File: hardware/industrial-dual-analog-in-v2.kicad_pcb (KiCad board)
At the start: 2 copper layers, 40 x 40 mm, 81 parts, among them P1 CON-SENSOR2, P2 CONN_1, P3 CONN_8, P4 DEBUG, P5 DEBUG, U1 LMV342IDRG4, U2 LM2664, U3 XMC1XXX24, U4 MCP3911, U5 DRILL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

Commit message: fix origin, fix logos
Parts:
- moved G*** 16.2 mm to (145.6, 100.0), turned to 90 degrees
- moved VAL 16.2 mm to (125.6, 100.0), turned to 90 degrees
- moved VAL 16.2 mm to (135.6, 100.0), turned to 90 degrees
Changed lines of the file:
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@@
-(kicad_pcb (version 4) (host pcbnew 4.0.7-e2-6376~58~ubuntu17.04.1)
+(kicad_pcb (version 4) (host pcbnew 4.0.7-e2-6376~61~ubuntu18.04.1)
   (general
     (links 158)
@@
     (pad_drill 0)
     (pad_to_mask_clearance 0.2)
-    (aux_axis_origin 0 0)
+    (aux_axis_origin 115.6 80)
+    (grid_origin 115.6 80)
     (visible_elements FFFFEF3F)
     (pcbplotparams
@@
     (descr "module 1 pin (ou trou mecanique de percage)")
     (tags DEV)
-    (fp_text reference P2 (at 0 -1.26746) (layer F.SilkS)
+    (fp_text reference P2 (at 0.8 -0.95) (layer F.SilkS) hide
       (effects (font (size 0.508 0.508) (thickness 0.127)))
     )
@@
   )
   (module kicad-libraries:CE_5mm (layer B.Cu)
-    (at 125.1 116.2 270)
-    (fp_text reference VAL (at 0 0 270) (layer B.SilkS) hide
+    (at 125.6 100 90)
+    (fp_text reference VAL (at 0 0 90) (layer B.SilkS) hide
       (effects (font (size 0.2 0.2) (thickness 0.05)) (justify mirror))
     )
-    (fp_text value CE_5mm (at 0 0 270) (layer B.SilkS) hide
+    (fp_text value CE_5mm (at 0 0 90) (layer B.SilkS) hide
       (effects (font (size 0.2 0.2) (thickness 0.05)) (justify mirror))
     )
@@
   )
   (module kicad-libraries:WEEE_7mm (layer B.Cu)
-    (at 135.6 116.2 270)
-    (fp_text reference VAL (at 0 0 270) (layer B.SilkS) hide
+    (at 135.6 100 90)
+    (fp_text reference VAL (at 0 0 90) (layer B.SilkS) hide
       (effects (font (size 0.2 0.2) (thickness 0.05)) (justify mirror))
     )
-    (fp_text value WEEE_7mm (at 0.75 0 270) (layer B.SilkS) hide
+    (fp_text value WEEE_7mm (at 0.75 0 90) (layer B.SilkS) hide
       (effects (font (size 0.2 0.2) (thickness 0.05)) (justify mirror))
     )
@@
   )
   (module kicad-libraries:Logo_CoMCU (layer B.Cu)
-    (at 146.1 116.2 270)
-    (fp_text reference G*** (at 0 0 270) (layer B.SilkS) hide
+    (at 145.6 100 90)
+    (fp_text reference G*** (at 0 0 90) (layer B.SilkS) hide
       (effects (font (thickness 0.3)) (justify mirror))
     )
-    (fp_text value LOGO (at 0.75 0 270) (layer B.SilkS) hide
+    (fp_text value LOGO (at 0.75 0 90) (layer B.SilkS) hide
       (effects (font (thickness 0.3)) (justify mirror))
     )

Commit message: Change capacitor footprint(s) to C0402F
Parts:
- C23: footprint kicad-libraries:C0402E -> kicad-libraries:C0402F
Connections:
- RP3 pad 3: (no net) -> Net-(RP3-Pad3)
- RP3 pad 6: (no net) -> Net-(RP3-Pad6)
- U3 pad 16: (no net) -> Net-(U3-Pad16)
- U3 pad 17: (no net) -> Net-(U3-Pad17)
- U3 pad 19: (no net) -> Net-(U3-Pad19)
- U3 pad 21: (no net) -> Net-(U3-Pad21)
- U3 pad 3: (no net) -> Net-(U3-Pad3)
- U3 pad 4: (no net) -> Net-(U3-Pad4)
- U3 pad 5: (no net) -> Net-(U3-Pad5)
- U3 pad 6: (no net) -> Net-(U3-Pad6)
- U3 pad 8: (no net) -> Net-(U3-Pad8)
- U4 pad 12: (no net) -> Net-(U4-Pad12)
- U4 pad 13: (no net) -> Net-(U4-Pad13)
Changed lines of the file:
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@@
-(kicad_pcb (version 4) (host pcbnew 4.0.7-e2-6376~61~ubuntu18.04.1)
+(kicad_pcb (version 4) (host pcbnew 4.0.2+dfsg1-stable)
   (general
     (links 158)
     (no_connects 1)
-    (area 17.19714 79.144999 156.455001 193.31)
+    (area 115.524999 79.924999 155.675001 120.075001)
     (thickness 1.6)
     (drawings 26)
@@
     (zones 0)
     (modules 81)
-    (nets 58)
+    (nets 71)
   )
   (page A4)
@@
   (layers
     (0 F.Cu signal)
-    (31 B.Cu signal hide)
+    (31 B.Cu signal)
     (32 B.Adhes user)
     (33 F.Adhes user)
@@
   (net 56 LED0)
   (net 57 LED1)
+  (net 58 "Net-(RP3-Pad3)")
+  (net 59 "Net-(RP3-Pad6)")
+  (net 60 "Net-(U3-Pad3)")
+  (net 61 "Net-(U3-Pad4)")
+  (net 62 "Net-(U3-Pad5)")
+  (net 63 "Net-(U3-Pad6)")
+  (net 64 "Net-(U3-Pad8)")
+  (net 65 "Net-(U3-Pad16)")
+  (net 66 "Net-(U3-Pad17)")
+  (net 67 "Net-(U3-Pad19)")
+  (net 68 "Net-(U3-Pad21)")
+  (net 69 "Net-(U4-Pad12)")
+  (net 70 "Net-(U4-Pad13)")
   (net_class Default "This is the default net class."
     (clearance 0.15)
@@
     (add_net "Net-(RP2-Pad7)")
     (add_net "Net-(RP2-Pad8)")
+    (add_net "Net-(RP3-Pad3)")
+    (add_net "Net-(RP3-Pad6)")
+    (add_net "Net-(U3-Pad16)")
+    (add_net "Net-(U3-Pad17)")
+    (add_net "Net-(U3-Pad19)")
+    (add_net "Net-(U3-Pad21)")
+    (add_net "Net-(U3-Pad3)")
+    (add_net "Net-(U3-Pad4)")
+    (add_net "Net-(U3-Pad5)")
+    (add_net "Net-(U3-Pad6)")
+    (add_net "Net-(U3-Pad8)")
+    (add_net "Net-(U4-Pad12)")
+    (add_net "Net-(U4-Pad13)")
     (add_net P0.2)
     (add_net S-CLK)
@@
     (pad 11 smd rect (at 2.925 -3.6 270) (size 0.45 1.75) (layers F.Cu F.Paste F.Mask)
       (net 7 DGND))
-    (pad 12 smd rect (at 2.275 -3.6 270) (size 0.45 1.75) (layers F.Cu F.Paste F.Mask))
-    (pad 13 smd rect (at 1.625 -3.6 270) (size 0.45 1.75) (layers F.Cu F.Paste F.Mask))
+    (pad 12 smd rect (at 2.275 -3.6 270) (size 0.45 1.75) (layers F.Cu F.Paste F.Mask)
+      (net 69 "Net-(U4-Pad12)"))
+    (pad 13 smd rect (at 1.625 -3.6 270) (size 0.45 1.75) (layers F.Cu F.Paste F.Mask)
+      (net 70 "Net-(U4-Pad13)"))
     (pad 14 smd rect (at 0.975 -3.6 270) (size 0.45 1.75) (layers F.Cu F.Paste F.Mask)
       (net 31 "Net-(R3-Pad2)"))
@@
     )
   )
-  (module kicad-libraries:C0402E (layer F.Cu)
-    (at 126.7 85.3 180)
-    (attr smd)
-    (fp_text reference C23 (at 0 0.125 180) (layer F.Fab)
-      (effects (font (size 0.2 0.2) (thickness 0.05)))
-    )
-    (fp_text value 220pF (at 0 -0.275 180) (layer F.Fab)
-      (effects (font (size 0.2 0.2) (thickness 0.05)))
-    )
-    (fp_line (start -0.8509 -0.44958) (end 0.8509 -0.44958) (layer F.Fab) (width 0.001))
-    (fp_line (start 0.8509 -0.44958) (end 0.8509 0.44958) (layer F.Fab) (width 0.001))
-    (fp_line (start 0.8509 0.44958) (end -0.8509 0.44958) (layer F.Fab) (width 0.001))
-    (fp_line (start -0.8509 0.44958) (end -0.8509 -0.44958) (layer F.Fab) (width 0.001))
-    (pad 1 smd rect (at -0.65 0 180) (size 0.7 0.9) (layers F.Cu F.Paste F.Mask)
-      (net 38 "Net-(C23-Pad1)"))
-    (pad 2 smd rect (at 0.65 0 180) (size 0.7 0.9) (layers F.Cu F.Paste F.Mask)
-      (net 7 DGND))
-    (model Capacitors_SMD/C_0402.wrl
-      (at (xyz 0 0 0))
-      (scale (xyz 1 1 1))
-      (rotate (xyz 0 0 0))
-    )
-  )
   (module kicad-libraries:QFN24-4x4mm-0.5mm (layer F.Cu)
     (at 121.71 87.72 90)
@@
     (pad 2 smd oval (at -2.025 -0.75 90) (size 1 0.3) (layers F.Cu F.Paste F.Mask)
       (net 39 "Net-(P4-Pad1)"))
-    (pad 3 smd oval (at -2.025 -0.25 90) (size 1 0.3) (layers F.Cu F.Paste F.Mask))
-    (pad 4 smd oval (at -2.025 0.25 90) (size 1 0.3) (layers F.Cu F.Paste F.Mask))
-    (pad 5 smd oval (at -2.025 0.75 90) (size 1 0.3) (layers F.Cu F.Paste F.Mask))
-    (pad 6 smd oval (at -2.025 1.25 90) (size 1 0.3) (layers F.Cu F.Paste F.Mask))
+    (pad 3 smd oval (at -2.025 -0.25 90) (size 1 0.3) (layers F.Cu F.Paste F.Mask)
+      (net 60 "Net-(U3-Pad3)"))
+    (pad 4 smd oval (at -2.025 0.25 90) (size 1 0.3) (layers F.Cu F.Paste F.Mask)
+      (net 61 "Net-(U3-Pad4)"))
+    (pad 5 smd oval (at -2.025 0.75 90) (size 1 0.3) (layers F.Cu F.Paste F.Mask)
+      (net 62 "Net-(U3-Pad5)"))
+    (pad 6 smd oval (at -2.025 1.25 90) (size 1 0.3) (layers F.Cu F.Paste F.Mask)
+      (net 63 "Net-(U3-Pad6)"))
     (pad 7 smd oval (at -1.25 2.025 180) (size 1 0.3) (layers F.Cu F.Paste F.Mask)
       (net 40 "Net-(P5-Pad2)"))
-    (pad 8 smd oval (at -0.75 2.025 180) (size 1 0.3) (layers F.Cu F.Paste F.Mask))
+    (pad 8 smd oval (at -0.75 2.025 180) (size 1 0.3) (layers F.Cu F.Paste F.Mask)
+      (net 64 "Net-(U3-Pad8)"))
     (pad 9 smd oval (at -0.25 2.025 180) (size 1 0.3) (layers F.Cu F.Paste F.Mask)
       (net 7 DGND))
@@
     (pad 15 smd oval (at 2.025 0.25 90) (size 1 0.3) (layers F.Cu F.Paste F.Mask)
       (net 55 LEDS))
-    (pad 16 smd oval (at 2.025 -0.25 90) (size 1 0.3) (layers F.Cu F.Paste F.Mask))
-    (pad 17 smd oval (at 2.025 -0.75 90) (size 1 0.3) (layers F.Cu F.Paste F.Mask))
+    (pad 16 smd oval (at 2.025 -0.25 90) (size 1 0.3) (layers F.Cu F.Paste F.Mask)
+      (net 65 "Net-(U3-Pad16)"))
+    (pad 17 smd oval (at 2.025 -0.75 90) (size 1 0.3) (layers F.Cu F.Paste F.Mask)
+      (net 66 "Net-(U3-Pad17)"))
     (pad 18 smd oval (at 2.025 -1.25 90) (size 1 0.3) (layers F.Cu F.Paste F.Mask)
       (net 42 S-MISO))
-    (pad 19 smd oval (at 1.25 -2.025 180) (size 1 0.3) (layers F.Cu F.Paste F.Mask))
+    (pad 19 smd oval (at 1.25 -2.025 180) (size 1 0.3) (layers F.Cu F.Paste F.Mask)
+      (net 67 "Net-(U3-Pad19)"))
     (pad 20 smd oval (at 0.75 -2.025 180) (size 1 0.3) (layers F.Cu F.Paste F.Mask)
       (net 45 S-CS))
-    (pad 21 smd oval (at 0.25 -2.025 180) (size 1 0.3) (layers F.Cu F.Paste F.Mask))
+    (pad 21 smd oval (at 0.25 -2.025 180) (size 1 0.3) (layers F.Cu F.Paste F.Mask)
+      (net 68 "Net-(U3-Pad21)"))
     (pad 22 smd oval (at -0.25 -2.025 180) (size 1 0.3) (layers F.Cu F.Paste F.Mask)
       (net 51 "Net-(RP2-Pad8)"))
@@
     (pad 2 smd rect (at -0.24892 0.575 270) (size 0.29972 0.65) (layers F.Cu F.Paste F.Mask)
       (net 54 "Net-(D5-Pad2)"))
-    (pad 3 smd rect (at 0.24892 0.575 270) (size 0.29972 0.65) (layers F.Cu F.Paste F.Mask))
+    (pad 3 smd rect (at 0.24892 0.575 270) (size 0.29972 0.65) (layers F.Cu F.Paste F.Mask)
+      (net 58 "Net-(RP3-Pad3)"))
     (pad 4 smd rect (at 0.7493 0.575 270) (size 0.29972 0.65) (layers F.Cu F.Paste F.Mask)
       (net 37 "Net-(D3-Pad2)"))
     (pad 5 smd rect (at 0.7493 -0.575 90) (size 0.29972 0.65) (layers F.Cu F.Paste F.Mask)
       (net 55 LEDS))
-    (pad 6 smd rect (at 0.24892 -0.575 90) (size 0.29972 0.65) (layers F.Cu F.Paste F.Mask))
+    (pad 6 smd rect (at 0.24892 -0.575 90) (size 0.29972 0.65) (layers F.Cu F.Paste F.Mask)
+      (net 59 "Net-(RP3-Pad6)"))
     (pad 7 smd rect (at -0.24892 -0.575 90) (size 0.29972 0.65) (layers F.Cu F.Paste F.Mask)
       (net 56 LED0))
@@
     )
   )
+  (module kicad-libraries:C0402F (layer F.Cu)
+    (at 126.7 85.3 180)
+    (fp_text reference C23 (at 0.1 0.15 180) (layer F.Fab)
+      (effects (font (size 0.2 0.2) (thickness 0.05)))
+    )
+    (fp_text value 220pF (at 0 -0.15 180) (layer F.Fab)
+      (effects (font (size 0.2 0.2) (thickness 0.05)))
+    )
+    (fp_line (start -0.9 -0.45) (end 0.9 -0.45) (layer F.Fab) (width 0.025))
+    (fp_line (start 0.9 -0.45) (end 0.9 0.45) (layer F.Fab) (width 0.025))
+    (fp_line (start 0.9 0.45) (end -0.9 0.45) (layer F.Fab) (width 0.025))
+    (fp_line (start -0.9 0.45) (end -0.9 -0.45) (layer F.Fab) (width 0.025))
+    (pad 2 smd rect (at 0.5 0 180) (size 0.6 0.7) (layers F.Cu F.Paste F.Mask)
+      (net 7 DGND))
+    (pad 1 smd rect (at -0.5 0 180) (size 0.6 0.7) (layers F.Cu F.Paste F.Mask)
+      (net 38 "Net-(C23-Pad1)"))
+    (model Capacitors_SMD/C_0402.wrl
+      (at (xyz 0 0 0))
+      (scale (xyz 1 1 1))
+      (rotate (xyz 0 0 0))
+    )
+  )

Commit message: specify processor
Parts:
- U3: value XMC1XXX24 -> XMC11XX24
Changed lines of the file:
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@@
-(kicad_pcb (version 4) (host pcbnew 4.0.2+dfsg1-stable)
+(kicad_pcb (version 4) (host pcbnew 4.0.7-e2-6376~61~ubuntu18.04.1)
   (general
     (links 158)
     (no_connects 1)
-    (area 115.524999 79.924999 155.675001 120.075001)
+    (area 17.19714 79.144999 156.455001 193.31)
     (thickness 1.6)
     (drawings 26)
@@
       (effects (font (size 0.3 0.3) (thickness 0.075)))
     )
-    (fp_text value XMC1XXX24 (at 0 0.8 90) (layer F.Fab)
+    (fp_text value XMC11XX24 (at 0 0.8 90) (layer F.Fab)
       (effects (font (size 0.3 0.3) (thickness 0.075)))
     )

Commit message: Fixed unconnected GND via and reroute 3V3-wire next to "Status"-marking
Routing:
- net 3V3: track 68.9 -> 68.3 mm
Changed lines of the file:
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@@
-(kicad_pcb (version 4) (host pcbnew 4.0.7-e2-6376~61~ubuntu18.04.1)
+(kicad_pcb (version 4) (host pcbnew 4.0.2+dfsg1-stable)
   (general
     (links 158)
-    (no_connects 1)
-    (area 17.19714 79.144999 156.455001 193.31)
+    (no_connects 0)
+    (area 115.524999 79.924999 155.675001 120.075001)
     (thickness 1.6)
     (drawings 26)
-    (tracks 654)
+    (tracks 660)
     (zones 0)
     (modules 81)
@@
   (via (at 139.05 97.1) (size 0.7) (layers F.Cu B.Cu) (net 3))
   (segment (start 138.6999 97.4501) (end 139.05 97.1) (width 0.35) (layer F.Cu) (net 3))
+  (segment (start 138.26 88.26) (end 142.02 84.5) (width 0.254) (layer B.Cu) (net 4))
+  (segment (start 142.02 84.5) (end 144.6 84.5) (width 0.254) (layer B.Cu) (net 4))
+  (segment (start 145.3 82.1) (end 144.95 81.75) (width 0.254) (layer F.Cu) (net 4))
+  (segment (start 145.3 83.7) (end 145.3 82.1) (width 0.254) (layer F.Cu) (net 4))
+  (via (at 145.3 83.7) (size 0.55) (drill 0.25) (layers F.Cu B.Cu) (net 4))
+  (segment (start 145.3 83.8) (end 145.3 83.7) (width 0.254) (layer B.Cu) (net 4))
+  (segment (start 144.6 84.5) (end 145.3 83.8) (width 0.254) (layer B.Cu) (net 4))
   (segment (start 147.3 81.75) (end 148.9 81.75) (width 0.25) (layer F.Cu) (net 4))
   (segment (start 144.95 81.75) (end 147.3 81.75) (width 0.25) (layer F.Cu) (net 4))
-  (segment (start 138.22 88.3) (end 142.02 84.5) (width 0.25) (layer B.Cu) (net 4))
+  (segment (start 138.22 88.3) (end 138.26 88.26) (width 0.25) (layer B.Cu) (net 4))
   (segment (start 144.95 81.75) (end 144.1 81.75) (width 0.25) (layer F.Cu) (net 4))
-  (segment (start 145.7 82.5) (end 144.95 81.75) (width 0.25) (layer F.Cu) (net 4))
-  (segment (start 145.7 83.9) (end 145.7 82.5) (width 0.25) (layer F.Cu) (net 4))
-  (segment (start 145.1 84.5) (end 145.7 83.9) (width 0.25) (layer F.Cu) (net 4))
-  (segment (start 142.9 84.5) (end 145.1 84.5) (width 0.25) (layer F.Cu) (net 4))
-  (via (at 142.9 84.5) (size 0.55) (drill 0.25) (layers F.Cu B.Cu) (net 4))
-  (segment (start 142.02 84.5) (end 142.9 84.5) (width 0.25) (layer B.Cu) (net 4))
   (segment (start 133.17 89.55) (end 125.5 89.55) (width 0.55) (layer B.Cu) (net 4))
   (segment (start 125.5 89.55) (end 125.5 93.5) (width 0.7) (layer B.Cu) (net 4))
@@
   (segment (start 119.17386 106.50114) (end 117.925 107.75) (width 0.7) (layer F.Cu) (net 36))
   (segment (start 119.7 106.50114) (end 119.17386 106.50114) (width 0.7) (layer F.Cu) (net 36))
+  (segment (start 127.275 80.7507) (end 127.8007 80.7507) (width 0.254) (layer F.Cu) (net 37))
+  (segment (start 129.2 80.97) (end 129.2 81) (width 0.254) (layer B.Cu) (net 37))
+  (segment (start 129.17 80.97) (end 129.2 80.97) (width 0.254) (layer B.Cu) (net 37))
+  (segment (start 129.14 80.94) (end 129.17 80.97) (width 0.254) (layer B.Cu) (net 37))
+  (segment (start 128.17 80.94) (end 129.14 80.94) (width 0.254) (layer B.Cu) (net 37))
+  (segment (start 128.13 80.9) (end 128.17 80.94) (width 0.254) (layer B.Cu) (net 37))
+  (via (at 128.13 80.9) (size 0.55) (drill 0.25) (layers F.Cu B.Cu) (net 37))
+  (segment (start 127.95 80.9) (end 128.13 80.9) (width 0.254) (layer F.Cu) (net 37))
+  (segment (start 127.8007 80.7507) (end 127.95 80.9) (width 0.254) (layer F.Cu) (net 37))
   (segment (start 131.4 80.8) (end 131.6 80.6) (width 0.25) (layer B.Cu) (net 37))
-  (segment (start 128.9 80.7) (end 129.3 81.1) (width 0.25) (layer B.Cu) (net 37))
+  (segment (start 129.2 81) (end 129.3 81.1) (width 0.25) (layer B.Cu) (net 37))
   (segment (start 129.3 81.1) (end 131.1 81.1) (width 0.25) (layer B.Cu) (net 37))
   (segment (start 131.1 81.1) (end 131.4 80.8) (width 0.25) (layer B.Cu) (net 37))
-  (segment (start 127.275 80.7507) (end 128.4493 80.7507) (width 0.25) (layer F.Cu) (net 37))
-  (via (at 128.5 80.7) (size 0.55) (drill 0.25) (layers F.Cu B.Cu) (net 37))
-  (segment (start 128.4493 80.7507) (end 128.5 80.7) (width 0.25) (layer F.Cu) (net 37))
-  (segment (start 128.5 80.7) (end 128.9 80.7) (width 0.25) (layer B.Cu) (net 37))
   (segment (start 141.2 83.3) (end 144.05 83.3) (width 0.25) (layer F.Cu) (net 37))
   (segment (start 138.5 80.6) (end 141.2 83.3) (width 0.25) (layer F.Cu) (net 37))

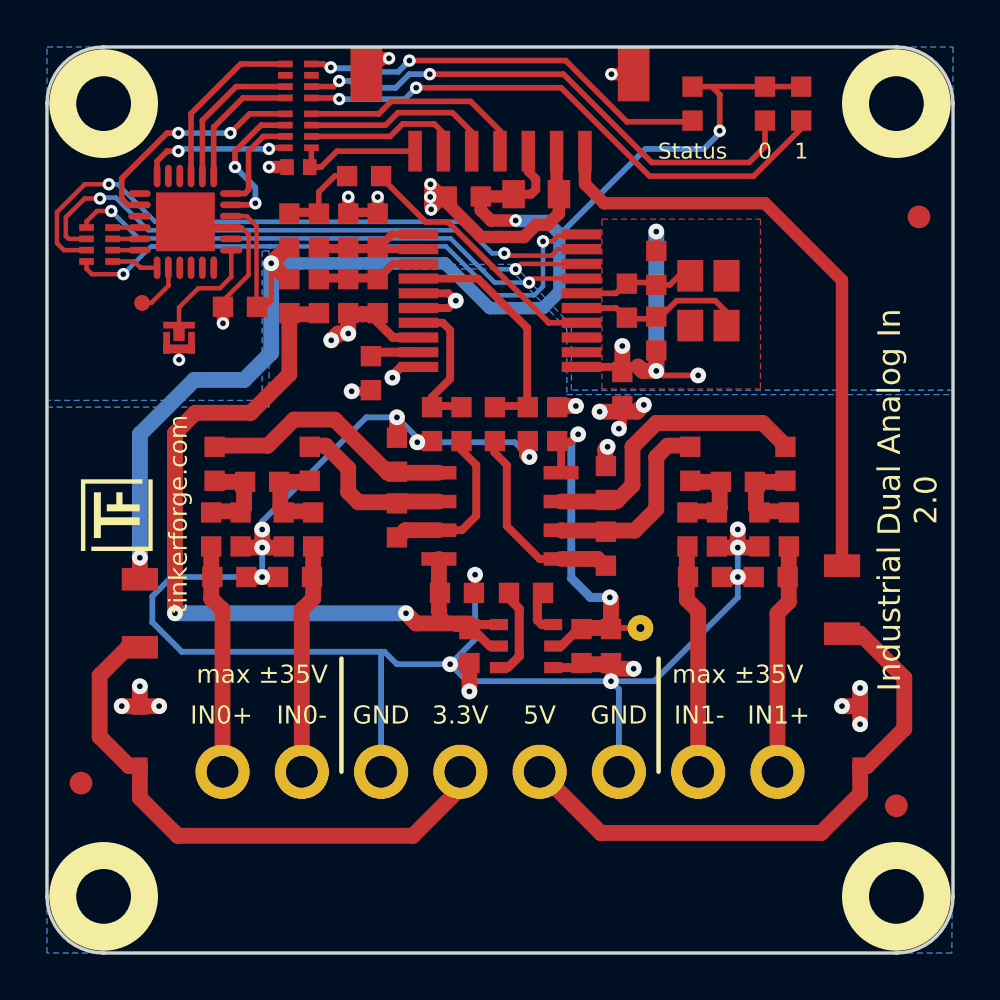
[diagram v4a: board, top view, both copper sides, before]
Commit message: add version 2.1 with 4MHz Crystal
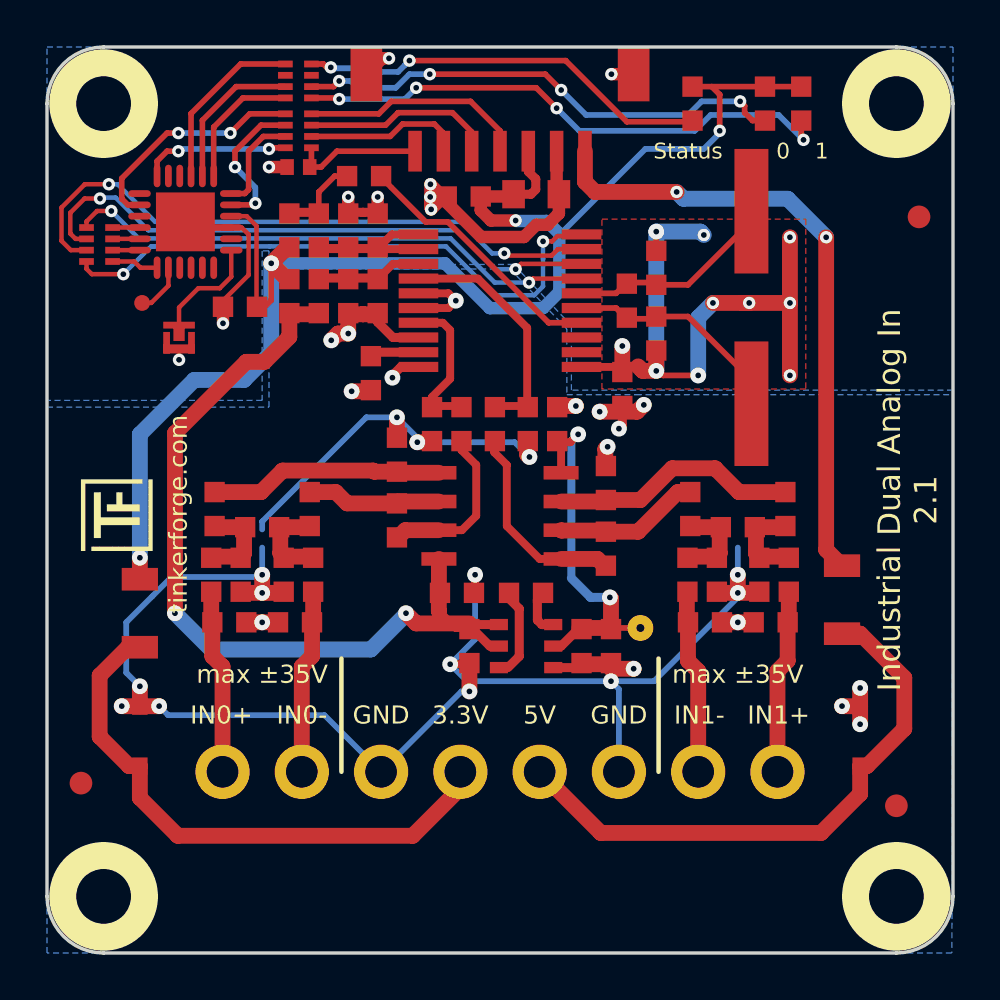
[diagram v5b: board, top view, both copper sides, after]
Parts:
- U3: value XMC11XX24 -> XMC1100
- X1: value 10MHz -> 4MHz; footprint kicad-libraries:CRYSTAL_3225 -> kicad-libraries:HC49_US
- moved C17 2.00 mm to (126.0, 103.3)
- moved C18 2.00 mm to (125.1, 101.2)
- moved C19 2.00 mm to (124.2, 103.3)
- moved C20 2.00 mm to (145.2, 103.3)
- moved C21 2.00 mm to (146.1, 101.2)
- moved C22 2.00 mm to (147.1, 103.3)
- moved G*** 2.00 mm to (145.6, 102.0)
- moved R13 2.00 mm to (127.2, 100.4)
- moved R14 2.00 mm to (123.0, 100.4)
- moved R15 2.00 mm to (144.0, 100.4)
- moved R16 2.00 mm to (148.2, 100.4)
- moved R17 2.00 mm to (127.3, 103.3)
- moved R18 2.00 mm to (122.8, 103.3)
- moved R19 2.00 mm to (143.9, 103.3)
- moved R20 2.00 mm to (148.3, 103.3)
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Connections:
- RP3 pad 3: Net-(RP3-Pad3) -> (no net)
- RP3 pad 6: Net-(RP3-Pad6) -> (no net)
- U3 pad 16: Net-(U3-Pad16) -> (no net)
- U3 pad 17: Net-(U3-Pad17) -> (no net)
- U3 pad 19: Net-(U3-Pad19) -> (no net)
- U3 pad 21: Net-(U3-Pad21) -> (no net)
- U3 pad 3: Net-(U3-Pad3) -> (no net)
- U3 pad 4: Net-(U3-Pad4) -> (no net)
- U3 pad 5: Net-(U3-Pad5) -> (no net)
- U3 pad 6: Net-(U3-Pad6) -> (no net)
- U3 pad 8: Net-(U3-Pad8) -> (no net)
- U4 pad 12: Net-(U4-Pad12) -> (no net)
- U4 pad 13: Net-(U4-Pad13) -> (no net)
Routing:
- net DGND: track 46.8 -> 62.2 mm, vias 14 -> 20
- net Net-(C8-Pad2): track 5.45 -> 9.59 mm
- net Net-(C9-Pad2): track 7.98 -> 10.2 mm
- net Net-(R15-Pad1): track 8.61 -> 6.41 mm
- net Net-(P3-Pad1): track 10.2 -> 8.16 mm
- net Net-(P3-Pad7): track 10.2 -> 8.16 mm
- net Net-(P3-Pad2): track 10.2 -> 8.16 mm
- net Net-(P3-Pad8): track 10.2 -> 8.16 mm
- net Net-(R11-Pad2): track 12.7 -> 10.9 mm
- net Net-(D5-Pad2): track 23.6 -> 22.0 mm, vias 2 -> 4
- net Net-(R13-Pad1): track 7.37 -> 5.92 mm
- net Net-(R10-Pad2): track 11.4 -> 10.3 mm
- net AGND: track 107.8 -> 108.5 mm
- net +5V: track 27.2 -> 27.8 mm, vias 0 -> 2
- net Net-(D4-Pad2): track 24.7 -> 25.1 mm, vias 2 -> 4
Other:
- board text added: "Copyright Tinkerforge GmbH 2019. This documentation describes Open Hardware and is licensed under the CERN OHL v. 1.1. You may redistribute and modify this documentation under the terms of the CERN OHL v.1.1. (http://ohwr.org/cernohl). This documentation is distributed WITHOUT ANY EXPRESS OR IMPLIED WARRANTY, INCLUDING OF MERCHANTABILITY, SATISFACTORY QUALITY AND FITNESS FOR A PARTICULAR PURPOSE.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"
- board text added: "Industrial Dual Analog In 2.1"
- board text removed: "Copyright Tinkerforge GmbH 2018. This documentation describes Open Hardware and is licensed under the CERN OHL v. 1.1. You may redistribute and modify this documentation under the terms of the CERN OHL v.1.1. (http://ohwr.org/cernohl). This documentation is distributed WITHOUT ANY EXPRESS OR IMPLIED WARRANTY, INCLUDING OF MERCHANTABILITY, SATISFACTORY QUALITY AND FITNESS FOR A PARTICULAR PURPOSE.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"
- board text removed: "Industrial Dual Analog In 2.0"
